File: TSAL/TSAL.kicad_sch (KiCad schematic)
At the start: 57 parts, among them J1 Conn_02x03_Counter_Clockwise, J2 Conn_01x02, J3 Conn_02x01, J4 Conn_02x01, Q1 BSS138, Q2 BSS138, Q3 AO3401A, U1 LM358, U10 74HC74, U12 4002, U13 7400, U2 74HC27, U3 74HC20, U4 4N35, U5 74HC08, U6 74HC86, U7 LM7805_TO220, U8 LM339, U9 LM339

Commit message: CREATE TSAL PCBs
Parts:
- removed TP1: TestPoint GRN+, Connector_Pin:Pin_D1.0mm_L10.0mm, symbol Connector:TestPoint
- removed U12: 4002, symbol 4xxx:4002
- removed U13: 7400, symbol 74xx:7400
- J2: footprint Connector_Molex:Molex_Micro-Fit_3.0_43650-0215_1x02_P3.00mm_Vertical -> Connector_Molex:Molex_Mini-Fit_Jr_5566-02A_2x01_P4.20mm_Vertical
- R16: footprint Resistor_SMD:R_0805_2012Metric_Pad1.20x1.40mm_HandSolder -> Resistor_SMD:R_0603_1608Metric_Pad0.98x0.95mm_HandSolder
- R21: footprint Resistor_SMD:R_0201_0603Metric_Pad0.64x0.40mm_HandSolder -> Resistor_SMD:R_0603_1608Metric_Pad0.98x0.95mm_HandSolder
- U2: footprint (none) -> Package_SO:SOIC-14_3.9x8.7mm_P1.27mm
- U3, U5, U6, U8, U9: footprint Package_SO:SOIC-14_3.9x8.7mm_P1.27mm -> Package_DIP:DIP-14_W7.62mm
- renumbered e to e1
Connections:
- net 5V: now also U8.3 (V+), U9.3 (V+)
- net 5V+_Iso: now also R33.1
- net GLV+: no longer U8.3 (V+), U9.3 (V+)
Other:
- company: (none) -> Formula Barton Racing
- title: (none) -> TSAL GREEN

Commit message: v1.0.1
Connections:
- net AIR+: now also J1.4 (Pin_4); no longer J1.6 (Pin_6)
- net AIR-: now also J1.1 (Pin_1); no longer J1.3 (Pin_3)
- net AIR-_Int: now also J1.6 (Pin_6); no longer J1.4 (Pin_4)
- net Precharge: now also J1.3 (Pin_3); no longer J1.1 (Pin_1)
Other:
- moved on the sheet: U2C
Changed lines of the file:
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@@
 	(wire
 		(pts
-			(xy 392.43 85.09) (xy 392.43 83.82)
+			(xy 388.62 85.09) (xy 388.62 83.82)
 		)
 		(stroke
@@
 	(wire
 		(pts
-			(xy 392.43 57.15) (xy 392.43 58.42)
+			(xy 388.62 57.15) (xy 388.62 58.42)
 		)
 		(stroke
@@
 		)
 	)
+	(label "AIR-"
+		(at 170.18 243.84 180)
+		(fields_autoplaced yes)
+		(effects
+			(font
+				(size 1.27 1.27)
+			)
+			(justify right bottom)
+		)
+	)
 	(label "SCS_Compliance"
 		(at 292.1 41.91 0)
@@
 	)
 	(label "5V"
-		(at 392.43 57.15 0)
+		(at 388.62 57.15 0)
 		(fields_autoplaced yes)
 		(effects
@@
 		)
 	)
-	(label "Precharge"
-		(at 170.18 243.84 180)
-		(fields_autoplaced yes)
-		(effects
-			(font
-				(size 1.27 1.27)
-			)
-			(justify right bottom)
-		)
-	)
 	(label "GRN+"
 		(at 205.74 238.76 0)
@@
 		)
 	)
+	(label "AIR+"
+		(at 186.69 248.92 0)
+		(fields_autoplaced yes)
+		(effects
+			(font
+				(size 1.27 1.27)
+			)
+			(justify left bottom)
+		)
+	)
 	(label "PreCh_Int"
 		(at 170.18 246.38 180)
@@
 		)
 	)
-	(label "HV+"
-		(at 63.5 66.04 180)
+	(label "Precharge"
+		(at 170.18 248.92 180)
 		(fields_autoplaced yes)
 		(effects
 			(font
 				(size 1.27 1.27)
-				(bold yes)
 			)
 			(justify right bottom)
 		)
 	)
-	(label "Precharge"
-		(at 269.24 57.15 270)
+	(label "AIR-_Int"
+		(at 186.69 243.84 0)
 		(fields_autoplaced yes)
 		(effects
@@
 				(size 1.27 1.27)
 			)
-			(justify right bottom)
+			(justify left bottom)
 		)
 	)
-	(label "AIR-_Int"
-		(at 248.92 58.42 270)
+	(label "HV+"
+		(at 63.5 66.04 180)
 		(fields_autoplaced yes)
 		(effects
 			(font
 				(size 1.27 1.27)
+				(bold yes)
 			)
 			(justify right bottom)
 		)
 	)
-	(label "AIR-"
-		(at 170.18 248.92 180)
+	(label "Precharge"
+		(at 269.24 57.15 270)
 		(fields_autoplaced yes)
 		(effects
@@
 		)
 	)
-	(label ".25V"
-		(at 284.48 58.42 270)
+	(label "AIR-_Int"
+		(at 248.92 58.42 270)
 		(fields_autoplaced yes)
 		(effects
 			(font
 				(size 1.27 1.27)
-				(thickness 0.254)
-				(bold yes)
 			)
 			(justify right bottom)
 		)
 	)
-	(label "AIR+"
-		(at 186.69 243.84 0)
+	(label ".25V"
+		(at 284.48 58.42 270)
 		(fields_autoplaced yes)
 		(effects
 			(font
 				(size 1.27 1.27)
+				(thickness 0.254)
+				(bold yes)
 			)
-			(justify left bottom)
+			(justify right bottom)
 		)
 	)
@@
 		)
 	)
-	(label "AIR-_Int"
-		(at 186.69 248.92 0)
-		(fields_autoplaced yes)
-		(effects
-			(font
-				(size 1.27 1.27)
-			)
-			(justify left bottom)
-		)
-	)
 	(label "GRN+"
 		(at 389.89 179.07 0)
@@
 		(on_board yes)
 		(dnp no)
-		(fields_autoplaced yes)
 		(property "Reference" "U5"
-			(at 377.19 69.8499 0)
+			(at 372.364 81.026 0)
 			(effects
 				(font
@@
 		)
 		(property "Value" "74HC08"
-			(at 377.19 72.3899 0)
+			(at 372.364 83.566 0)
 			(effects
 				(font
@@
 	(symbol
 		(lib_id "power:+12V")
-		(at 392.43 85.09 180)
+		(at 388.62 85.09 180)
 		(unit 1)
 		(exclude_from_sim no)
@@
 		(dnp no)
 		(property "Reference" "#PWR020"
-			(at 392.43 81.28 0)
+			(at 388.62 81.28 0)
 			(effects
 				(font
@@
 		)
 		(property "Value" "GLV-"
-			(at 392.43 88.138 90)
+			(at 388.62 88.138 90)
 			(effects
 				(font
@@
 		)
 		(property "Footprint" ""
-			(at 392.43 85.09 0)
+			(at 388.62 85.09 0)
 			(effects
 				(font
@@
 		)
 		(property "Datasheet" ""
-			(at 392.43 85.09 0)
+			(at 388.62 85.09 0)
 			(effects
 				(font
@@
 		)
 		(property "Description" ""
-			(at 392.43 85.09 0)
+			(at 388.62 85.09 0)
 			(effects
 				(font
@@
 		(dnp no)
 		(property "Reference" "U3"
-			(at 314.452 80.772 0)
+			(at 323.088 80.518 0)
 			(effects
 				(font
@@
 		)
 		(property "Value" "74HC20"
-			(at 314.452 83.312 0)
+			(at 323.088 83.058 0)
 			(effects
 				(font
@@
 		(lib_name "4002_3")
 		(lib_id "4xxx:4002")
-		(at 392.43 71.12 0)
+		(at 388.62 71.12 0)
 		(unit 3)
 		(exclude_from_sim no)
@@
 		(dnp no)
 		(property "Reference" "U2"
-			(at 401.066 70.358 0)
+			(at 392.938 80.772 0)
 			(effects
 				(font
@@
 		)
 		(property "Value" "74HC27"
-			(at 401.066 72.898 0)
+			(at 392.938 83.312 0)
 			(effects
 				(font
@@
 		)
 		(property "Footprint" "Package_SO:SOIC-14_3.9x8.7mm_P1.27mm"
-			(at 392.43 71.12 0)
+			(at 388.62 71.12 0)
 			(effects
 				(font
@@
 		)
 		(property "Datasheet" "https://assets.nexperia.com/documents/data-sheet/74HC_HCT27.pdf"
-			(at 392.43 71.12 0)
+			(at 388.62 71.12 0)
 			(effects
 				(font
@@
 		)
 		(property "Description" "Dual  4 input NOR gate"
-			(at 392.43 71.12 0)
+			(at 388.62 71.12 0)
 			(effects
 				(font

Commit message: Modify TSAL PCB and use relative paths for libraries
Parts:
- removed unit 4 of U5
- added C5: .33uF, Capacitor_SMD:C_0603_1608Metric_Pad1.08x0.95mm_HandSolder, symbol Device:C
- added C6: 0.1uF, Capacitor_SMD:C_0603_1608Metric_Pad1.08x0.95mm_HandSolder, symbol Device:C
- R11: value 19.1K -> 100K
- R12: value 1K -> 5.1K
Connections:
- net 5V: now also C6.2
- net GLV+: now also C5.1
- net GLV-: now also C5.2, C6.1
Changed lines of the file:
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@@
 	)
 	(junction
+		(at 330.2 44.45)
+		(diameter 0)
+		(color 0 0 0 0)
+	)
+	(junction
 		(at 158.75 71.12)
 		(diameter 0)
@@
 	)
 	(junction
+		(at 341.63 36.83)
+		(diameter 0)
+		(color 0 0 0 0)
+	)
+	(junction
+		(at 320.04 36.83)
+		(diameter 0)
+		(color 0 0 0 0)
+	)
+	(junction
 		(at 350.52 152.4)
 		(diameter 0)
@@
 	(wire
 		(pts
+			(xy 320.04 44.45) (xy 330.2 44.45)
+		)
+		(stroke
+			(width 0)
+			(type default)
+		)
+	)
+	(wire
+		(pts
 			(xy 287.02 41.91) (xy 292.1 41.91)
 		)
@@
 	(wire
 		(pts
+			(xy 330.2 44.45) (xy 341.63 44.45)
+		)
+		(stroke
+			(width 0)
+			(type default)
+		)
+	)
+	(wire
+		(pts
 			(xy 63.5 123.19) (xy 66.04 123.19)
 		)
@@
 	(text "Fault Latch"
 		(exclude_from_sim no)
-		(at 309.372 151.384 0)
+		(at 307.34 152.146 0)
 		(effects
 			(font
@@
 			)
 		)
-		(property "Value" "1K"
+		(property "Value" "5.1K"
 			(at 364.49 44.4499 0)
 			(effects
@@
 	)
 	(symbol
+		(lib_id "Device:C")
+		(at 320.04 40.64 0)
+		(unit 1)
+		(exclude_from_sim no)
+		(in_bom yes)
+		(on_board yes)
+		(dnp no)
+		(property "Reference" "C5"
+			(at 314.198 40.64 0)
+			(effects
+				(font
+					(size 1.27 1.27)
+				)
+				(justify left)
+			)
+		)
+		(property "Value" ".33uF"
+			(at 314.198 43.18 0)
+			(effects
+				(font
+					(size 1.27 1.27)
+				)
+				(justify left)
+			)
+		)
+		(property "Footprint" "Capacitor_SMD:C_0603_1608Metric_Pad1.08x0.95mm_HandSolder"
+			(at 321.0052 44.45 0)
+			(effects
+				(font
+					(size 1.27 1.27)
+				)
+				(hide yes)
+			)
+		)
+		(property "Datasheet" "~"
+			(at 320.04 40.64 0)
+			(effects
+				(font
+					(size 1.27 1.27)
+				)
+				(hide yes)
+			)
+		)
+		(property "Description" "Unpolarized capacitor"
+			(at 320.04 40.64 0)
+			(effects
+				(font
+					(size 1.27 1.27)
+				)
+				(hide yes)
+			)
+		)
+		(pin "1"
+		)
+		(pin "2"
+		)
+		(instances
+			(project "TSAL"
+				(path "/3dba08e1-8d4d-49dd-80dc-41df92bd5b0c"
+					(reference "C5")
+					(unit 1)
+				)
+			)
+		)
+	)
+	(symbol
 		(lib_id "74xx:74LS20")
 		(at 200.66 118.11 0)
@@
 			)
 		)
-		(property "Value" "19.1K"
+		(property "Value" "100K"
 			(at 364.49 34.2899 0)
 			(effects
@@
 	)
 	(symbol
+		(lib_id "Device:C")
+		(at 341.63 40.64 180)
+		(unit 1)
+		(exclude_from_sim no)
+		(in_bom yes)
+		(on_board yes)
+		(dnp no)
+		(property "Reference" "C6"
+			(at 336.804 42.672 0)
+			(effects
+				(font
+					(size 1.27 1.27)
+				)
+				(justify right)
+			)
+		)
+		(property "Value" "0.1uF"
+			(at 336.804 45.212 0)
+			(effects
+				(font
+					(size 1.27 1.27)
+				)
+				(justify right)
+			)
+		)
+		(property "Footprint" "Capacitor_SMD:C_0603_1608Metric_Pad1.08x0.95mm_HandSolder"
+			(at 340.6648 36.83 0)
+			(effects
+				(font
+					(size 1.27 1.27)
+				)
+				(hide yes)
+			)
+		)
+		(property "Datasheet" "~"
+			(at 341.63 40.64 0)
+			(effects
+				(font
+					(size 1.27 1.27)
+				)
+				(hide yes)
+			)
+		)
+		(property "Description" "Unpolarized capacitor"
+			(at 341.63 40.64 0)
+			(effects
+				(font
+					(size 1.27 1.27)
+				)
+				(hide yes)
+			)
+		)
+		(pin "1"
+		)
+		(pin "2"
+		)
+		(instances
+			(project "TSAL"
+				(path "/3dba08e1-8d4d-49dd-80dc-41df92bd5b0c"
+					(reference "C6")
+					(unit 1)
+				)
+			)
+		)
+	)
+	(symbol
 		(lib_id "Regulator_Linear:LM7805_TO220")
 		(at 330.2 36.83 0)
@@
 					(unit 4)
 				)
-			)
-		)
-	)
-	(symbol
-		(lib_id "4xxx:4081")
-		(at 434.34 165.1 0)
-		(unit 4)
-		(exclude_from_sim no)
-		(in_bom yes)
-		(on_board yes)
-		(dnp no)
-		(fields_autoplaced yes)
-		(property "Reference" "U5"
-			(at 434.3317 156.21 0)
-			(effects
-				(font
-					(size 1.27 1.27)
-				)
-			)
-		)
-		(property "Value" "74HC08"
-			(at 434.3317 158.75 0)
-			(effects
-				(font
-					(size 1.27 1.27)
-				)
-			)
-		)
-		(property "Footprint" "Package_DIP:DIP-14_W7.62mm"
-			(at 434.34 165.1 0)
-			(effects
-				(font
-					(size 1.27 1.27)
-				)
-				(hide yes)
-			)
-		)
-		(property "Datasheet" "http://www.intersil.com/content/dam/Intersil/documents/cd40/cd4073bms-81bms-82bms.pdf"
-			(at 434.34 165.1 0)
-			(effects
-				(font
-					(size 1.27 1.27)
-				)
-				(hide yes)
-			)
-		)
-		(property "Description" "Quad And 2 inputs"
-			(at 434.34 165.1 0)
-			(effects
-				(font
-					(size 1.27 1.27)
-				)
-				(hide yes)
-			)
-		)
-		(pin "8"
-		)
-		(pin "6"
-		)
-		(pin "1"
-		)
-		(pin "10"
-		)
-		(pin "13"
-		)
-		(pin "14"
-		)
-		(pin "12"
-		)
-		(pin "9"
-		)
-		(pin "3"
-		)
-		(pin "7"
-		)
-		(pin "11"
-		)
-		(pin "5"
-		)
-		(pin "4"
-		)
-		(pin "2"
-		)
-		(instances
-			(project ""
-				(path "/3dba08e1-8d4d-49dd-80dc-41df92bd5b0c"
-					(reference "U5")
-					(unit 4)
-				)

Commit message: minor changes
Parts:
- removed C1: 0.1 uF, Capacitor_SMD:C_0805_2012Metric, symbol Device:C
- removed D1: 2.4V, Diode_THT:D_DO-35_SOD27_P7.62mm_Horizontal, symbol Device:D_Zener
- removed R1, R2: 5.6K, Resistor_SMD:R_2512_6332Metric_Pad1.40x3.35mm_HandSolder, symbol Device:R
- removed R3: 6.8K, Resistor_SMD:R_2512_6332Metric_Pad1.40x3.35mm_HandSolder, symbol Device:R
- removed R4: 2.7K, Resistor_SMD:R_2512_6332Metric_Pad1.40x3.35mm_HandSolder, symbol Device:R
- removed unit 2 of U10
- removed unit 2 of U2
- removed unit 2 of U3
- removed unit 4 of U6
- removed unit 4 of U8
- removed unit 3 of U8
- added R22: 500K, Resistor_SMD:R_0603_1608Metric_Pad0.98x0.95mm_HandSolder, symbol Device:R
- R16: value 500 -> 390
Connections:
- net GLV-: now also R22.1
- net at C4.1, R20.2, U10.4 (~{S}): now also R22.2
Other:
- note added: "TODO: Try Implementing the latch using opamps from u10 and save one IC"
- note removed: "1W resistors"
- note removed: "HV Supply and Ref"
- note removed: "Mini-Fit_Jr_02A"
- moved on the sheet: C4, e1

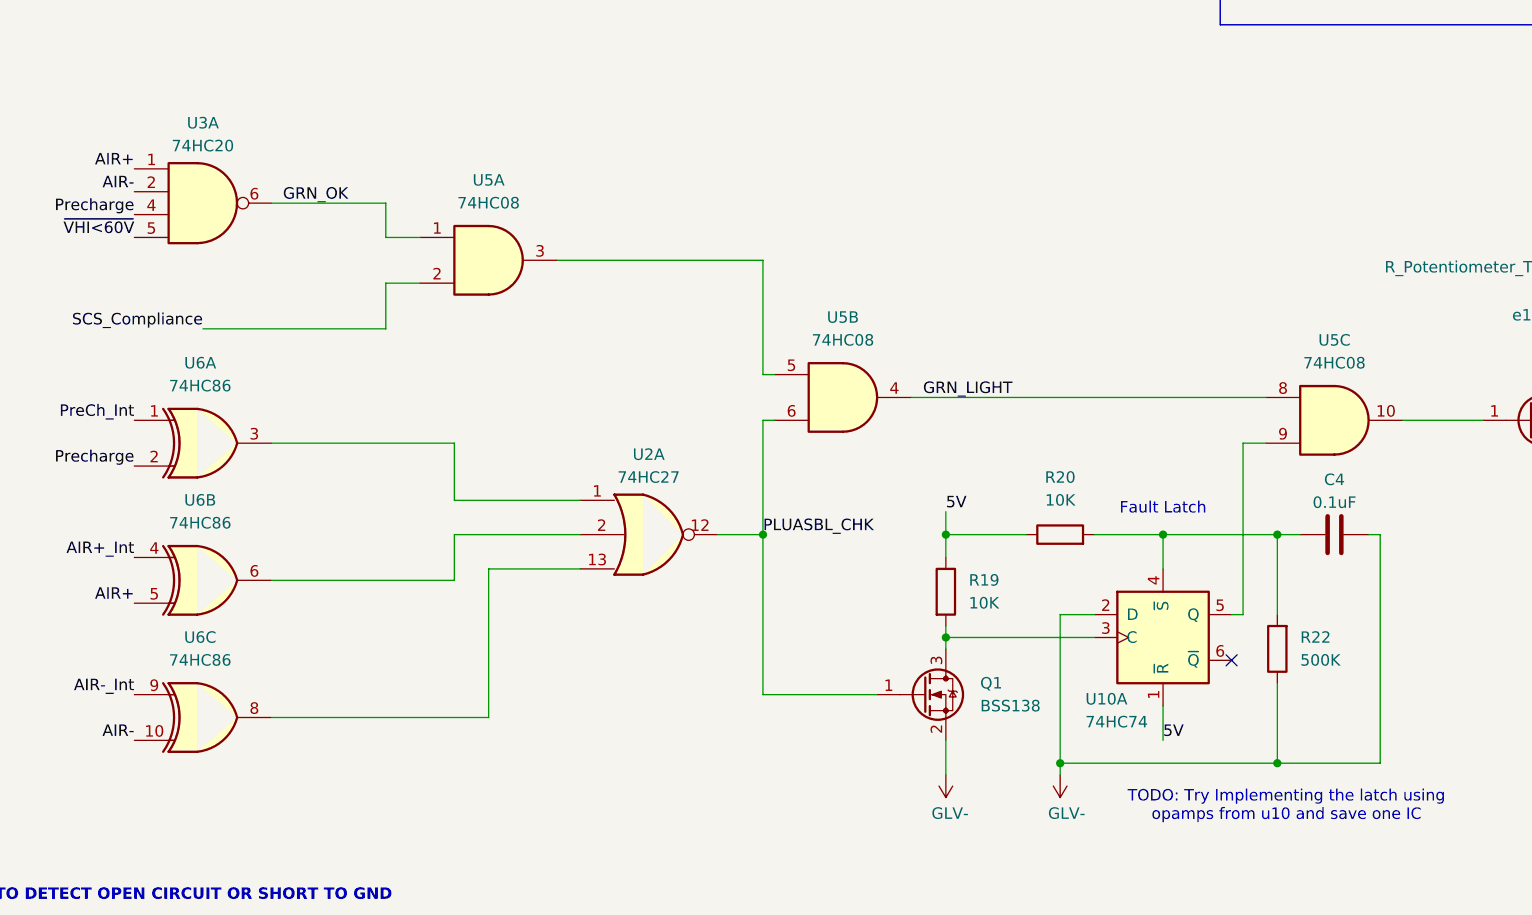
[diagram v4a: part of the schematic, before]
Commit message: Updated to KiCad v9
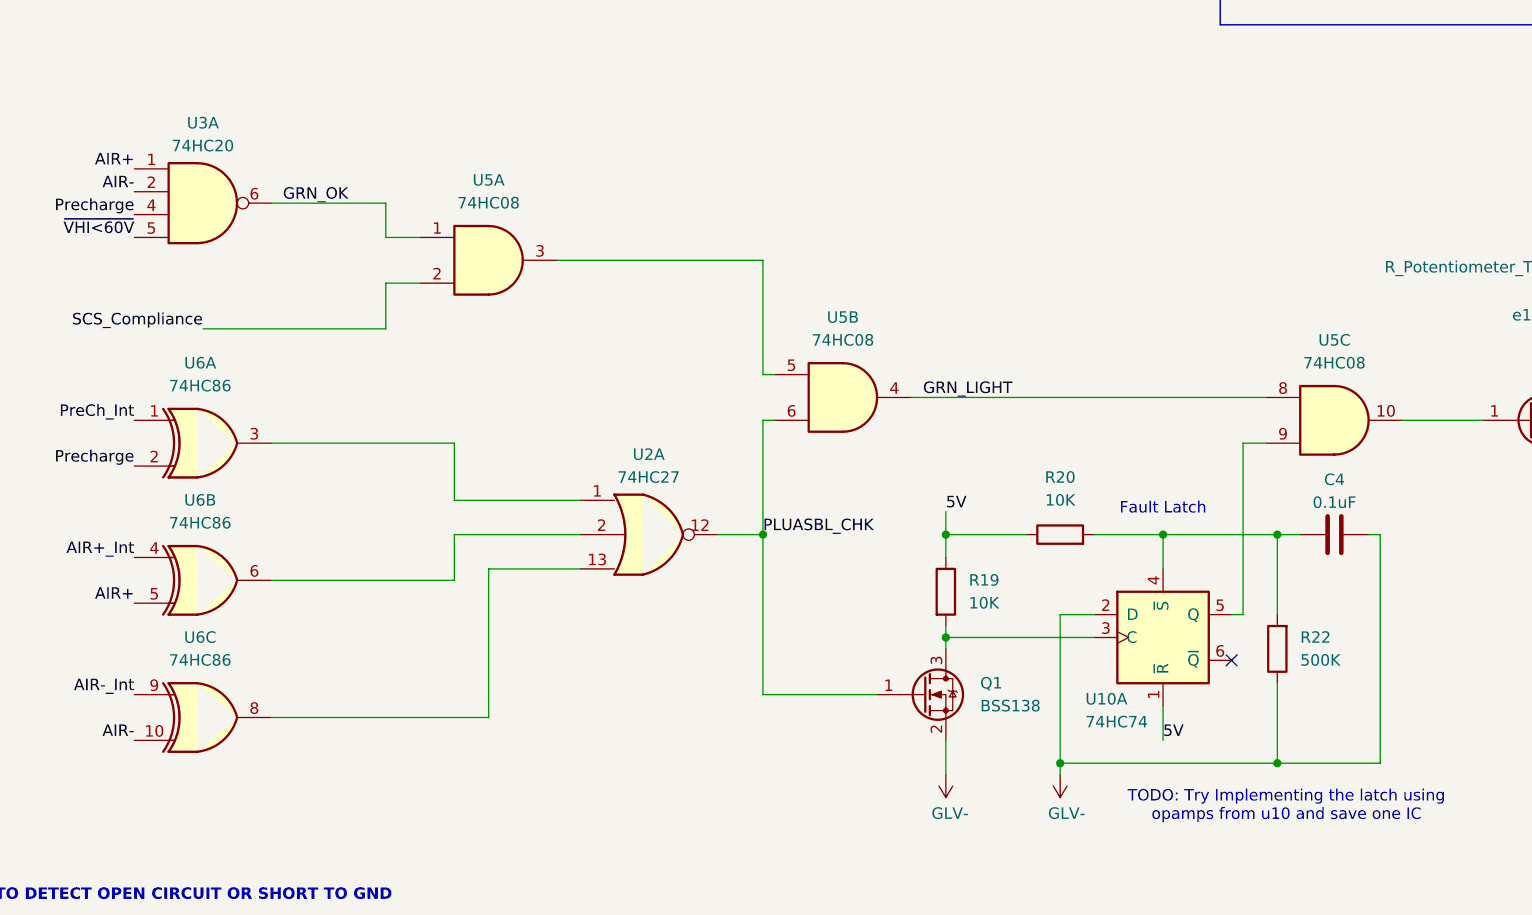
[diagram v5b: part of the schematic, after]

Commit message: Add latest circuit PDFs
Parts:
- added C10, C11, C12, C7, C8, C9: 0.1uF, Capacitor_SMD:C_0603_1608Metric_Pad1.08x0.95mm_HandSolder, symbol Device:C
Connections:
- net AIR+: now also C7.1
- net AIR+_Int: now also C8.1
- net AIR-: now also C12.1
- net AIR-_Int: now also C9.1
- net GLV-: now also C10.2, C11.2, C12.2, C7.2, C8.2, C9.2
- net PreCh_Int: now also C11.1
- net Precharge: now also C10.1
